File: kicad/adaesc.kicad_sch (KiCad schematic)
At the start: 8 parts, among them J1 JST_02, Q1 IRFZ44N, Q2 IRFZ44N, Q3 IRFZ44N, Q4 IRFZ44N, Q5 IRFZ44N, Q6 IRFZ44N

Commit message: better option
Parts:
- removed A1: Arduino_Pro_Mini(with_programming_pins), PCM_SL_Development_Boards:Arduino_Pro_Mini(with_programming_pins), symbol PCM_SL_Development_Board:Arduino_Pro_Mini(with_programming_pins)
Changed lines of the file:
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@@
-		)
-	)
-	(symbol
-		(lib_id "PCM_SL_Development_Board:Arduino_Pro_Mini(with_programming_pins)")
-		(at 73.66 99.06 0)
-		(unit 1)
-		(exclude_from_sim no)
-		(in_bom yes)
-		(on_board yes)
-		(dnp no)
-		(fields_autoplaced yes)
-		(property "Reference" "A1"
-			(at 83.4741 69.85 0)
-			(effects
-				(font
-					(size 1.27 1.27)
-				)
-				(justify left)
-			)
-		)
-		(property "Value" "Arduino_Pro_Mini(with_programming_pins)"
-			(at 83.4741 72.39 0)
-			(effects
-				(font
-					(size 1.27 1.27)
-				)
-				(justify left)
-			)
-		)
-		(property "Footprint" "PCM_SL_Development_Boards:Arduino_Pro_Mini(with_programming_pins)"
-			(at 74.93 104.14 0)
-			(effects
-				(font
-					(size 1.27 1.27)
-				)
-				(hide yes)
-			)
-		)
-		(property "Datasheet" ""
-			(at 74.93 58.42 0)
-			(effects
-				(font
-					(size 1.27 1.27)
-				)
-				(hide yes)
-			)
-		)
-		(property "Description" "Arduino pro mini Development Board with programming pins"
-			(at 73.66 99.06 0)
-			(effects
-				(font
-					(size 1.27 1.27)
-				)
-				(hide yes)
-			)
-		)
-		(pin "21"
-		)
-		(pin "29"
-		)
-		(pin "24"
-		)
-		(pin "10"
-		)
-		(pin "1"
-		)
-		(pin "4"
-		)
-		(pin "33"
-		)
-		(pin "30"
-		)
-		(pin "32"
-		)
-		(pin "31"
-		)
-		(pin "26"
-		)
-		(pin "9"
-		)
-		(pin "11"
-		)
-		(pin "7"
-		)
-		(pin "18"
-		)
-		(pin "6"
-		)
-		(pin "8"
-		)
-		(pin "13"
-		)
-		(pin "14"
-		)
-		(pin "27"
-		)
-		(pin "17"
-		)
-		(pin "20"
-		)
-		(pin "22"
-		)
-		(pin "3"
-		)
-		(pin "5"
-		)
-		(pin "28"
-		)
-		(pin "23"
-		)
-		(pin "2"
-		)
-		(pin "19"
-		)
-		(pin "16"
-		)
-		(pin "15"
-		)
-		(pin "12"
-		)
-		(instances
-			(project ""
-				(path "/ea6e46f4-792c-4833-a2be-5b224bd6501d"
-					(reference "A1")
-					(unit 1)
-				)
-			)
 		)
 	)

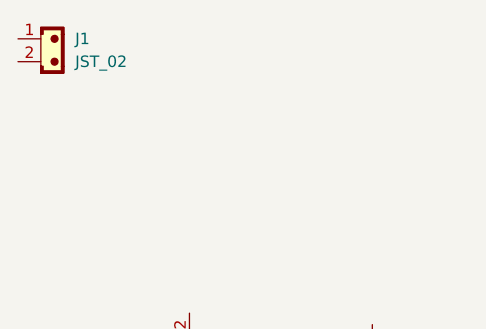
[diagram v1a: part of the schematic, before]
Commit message: deleted thingy
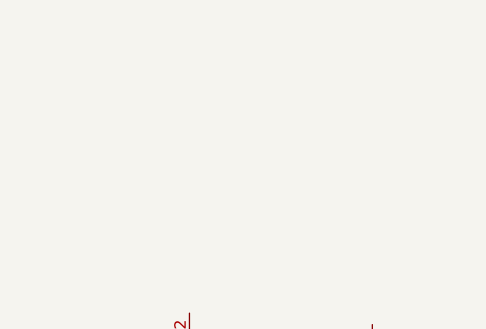
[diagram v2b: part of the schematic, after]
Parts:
- removed J1: JST_02, Connector_JST:JST_EH_B2B-EH-A_1x02_P2.50mm_Vertical, symbol PCM_SL_Connectors:JST_02
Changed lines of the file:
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@@
-	)
-	(symbol
-		(lib_id "PCM_SL_Connectors:JST_02")
-		(at 118.11 55.88 0)
-		(unit 1)
-		(exclude_from_sim no)
-		(in_bom yes)
-		(on_board yes)
-		(dnp no)
-		(fields_autoplaced yes)
-		(property "Reference" "J1"
-			(at 120.65 54.6099 0)
-			(effects
-				(font
-					(size 1.27 1.27)
-				)
-				(justify left)
-			)
-		)
-		(property "Value" "JST_02"
-			(at 120.65 57.1499 0)
-			(effects
-				(font
-					(size 1.27 1.27)
-				)
-				(justify left)
-			)
-		)
-		(property "Footprint" "Connector_JST:JST_EH_B2B-EH-A_1x02_P2.50mm_Vertical"
-			(at 118.11 49.53 0)
-			(effects
-				(font
-					(size 1.27 1.27)
-				)
-				(hide yes)
-			)
-		)
-		(property "Datasheet" ""
-			(at 118.11 49.53 0)
-			(effects
-				(font
-					(size 1.27 1.27)
-				)
-				(hide yes)
-			)
-		)
-		(property "Description" "JST Connector  2 pins"
-			(at 118.11 55.88 0)
-			(effects
-				(font
-					(size 1.27 1.27)
-				)
-				(hide yes)
-			)
-		)
-		(pin "1"
-		)
-		(pin "2"
-		)
-		(instances
-			(project ""
-				(path "/ea6e46f4-792c-4833-a2be-5b224bd6501d"
-					(reference "J1")
-					(unit 1)
-				)
-			)
-		)
 	)
 	(symbol

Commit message: :P
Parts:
- added J1, J2, J3: Conn_01x01_MountingPin, symbol Connector_Generic_MountingPin:Conn_01x01_MountingPin
- added J10, J9: Conn_01x07_MountingPin, symbol Connector_Generic_MountingPin:Conn_01x07_MountingPin
- added J6, J7, J8: Conn_01x03_MountingPin, symbol Connector_Generic_MountingPin:Conn_01x03_MountingPin
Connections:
- net +12V: now reaches Q6.1 (G)
- net +12V: now also Q4.1 (G), Q5.1 (G)
- net at Q6.2 (D): now also J10.D5
- net at Q6.3 (S): now also Q4.3 (S), J1.1 (Pin_1)
- net at Q4.2 (D): now also J10.D3
- net at Q5.2 (D): now also J10.D4
- net at Q5.3 (S): now also Q2.3 (S), J2.1 (Pin_1)
- net GND: now reaches Q1.1 (G)
- net GND: now also Q2.1 (G), Q3.1 (G)
- net at Q1.2 (D): now also J10.D0
- net at Q1.3 (S): now also Q3.3 (S), J3.1 (Pin_1)
- net at Q2.2 (D): now also J10.D1
- net at Q3.2 (D): now also J10.D2
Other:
- moved on the sheet: Q1, Q2, Q3, Q4, Q5, Q6
